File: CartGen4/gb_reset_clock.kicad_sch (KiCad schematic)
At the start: 7 parts, among them SW1 SW_Push, U2 SN74LV1T34DCKR, U3 SIT8008BI-73-33E-33.333333G

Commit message: Changed most R and C to 0402 size
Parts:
- C18: footprint Capacitor_SMD:C_0603_1608Metric_Pad1.08x0.95mm_HandSolder -> Capacitor_SMD:C_0402_1005Metric_Pad0.74x0.62mm_HandSolder
- R11, R13: footprint Resistor_SMD:R_0603_1608Metric_Pad0.98x0.95mm_HandSolder -> Resistor_SMD:R_0402_1005Metric_Pad0.72x0.64mm_HandSolder
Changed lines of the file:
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@@
     (property "Reference" "R13" (id 0) (at 57.15 54.61 90))
     (property "Value" "1K" (id 1) (at 57.15 57.15 90))
-    (property "Footprint" "Resistor_SMD:R_0603_1608Metric_Pad0.98x0.95mm_HandSolder" (id 2) (at 57.15 62.738 90)
+    (property "Footprint" "Resistor_SMD:R_0402_1005Metric_Pad0.72x0.64mm_HandSolder" (id 2) (at 57.15 62.738 90)
       (effects (font (size 1.27 1.27)) hide)
     )
@@
       (effects (font (size 1.27 1.27)) (justify left))
     )
-    (property "Footprint" "Capacitor_SMD:C_0603_1608Metric_Pad1.08x0.95mm_HandSolder" (id 2) (at 112.7252 73.66 0)
+    (property "Footprint" "Capacitor_SMD:C_0402_1005Metric_Pad0.74x0.62mm_HandSolder" (id 2) (at 112.7252 73.66 0)
       (effects (font (size 1.27 1.27)) hide)
     )
@@
       (effects (font (size 1.27 1.27)) (justify right))
     )
-    (property "Footprint" "Resistor_SMD:R_0603_1608Metric_Pad0.98x0.95mm_HandSolder" (id 2) (at 53.848 127 90)
-      (effects (font (size 1.27 1.27)) hide)
-    )
+    (property "Footprint" "Resistor_SMD:R_0402_1005Metric_Pad0.72x0.64mm_HandSolder" (id 2) (at 53.848 127 90)
+      (effects (font (size 1.27 1.27)) hide)
+    )

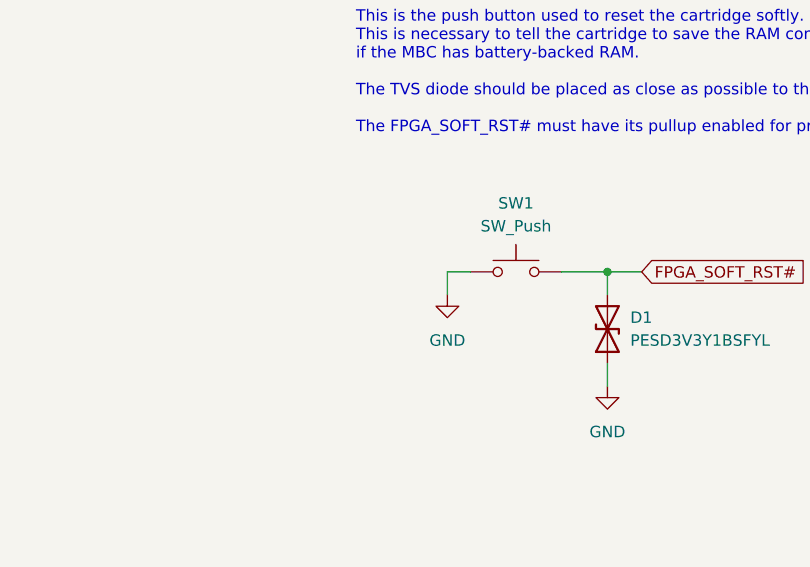
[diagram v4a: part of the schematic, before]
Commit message: Wired general purpose signals
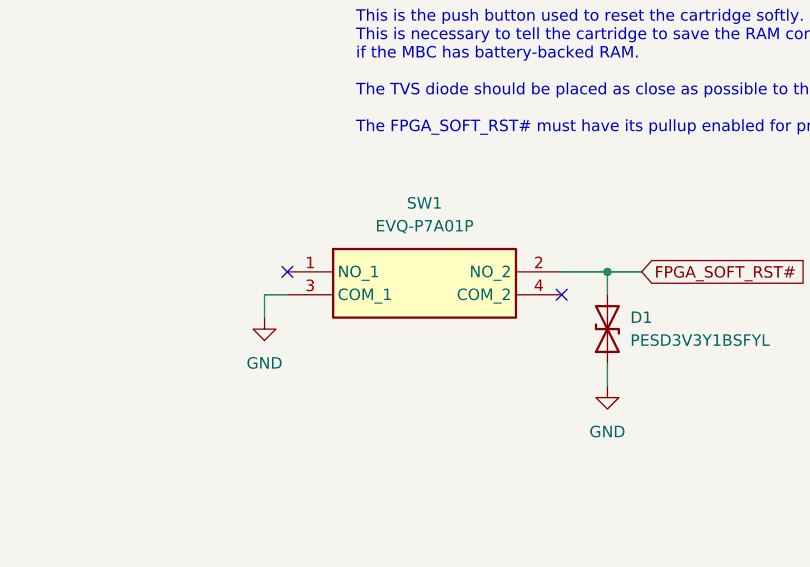
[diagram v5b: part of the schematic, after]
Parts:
- removed SW1: SW_Push, Button_Switch_SMD:SW_SPST_TL3305A, symbol Switch:SW_Push
- added SW1: EVQ-P7A01P, SamacSys_Parts:EVQP7J01P, symbol SamacSys_Parts:EVQ-P7A01P
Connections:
- net FPGA_SOFT_RST#: now also SW1.2 (NO_2)
- net GND: now also SW1.3 (COM_1)
- no-connect marks 0 -> 2
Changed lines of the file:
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@@
   (junction (at 52.07 120.65) (diameter 0) (color 0 0 0 0)
   )
+  (no_connect (at 163.83 66.04))
+  (no_connect (at 194.31 68.58))
   (wire (pts (xy 90.17 63.5) (xy 92.71 63.5))
     (stroke (width 0) (type default) (color 0 0 0 0))
@@
     (stroke (width 0) (type default) (color 0 0 0 0))
   )
-  (wire (pts (xy 181.61 66.04) (xy 181.61 68.58))
-    (stroke (width 0) (type default) (color 0 0 0 0))
-  )
-  (wire (pts (xy 184.15 66.04) (xy 181.61 66.04))
+  (wire (pts (xy 161.29 68.58) (xy 161.29 71.12))
+    (stroke (width 0) (type default) (color 0 0 0 0))
+  )
+  (wire (pts (xy 163.83 68.58) (xy 161.29 68.58))
     (stroke (width 0) (type default) (color 0 0 0 0))
   )
@@
     (pin "1")
   )
-  (symbol (lib_id "power:GND") (at 181.61 68.58 0) (unit 1)
-    (in_bom yes) (on_board yes) (fields_autoplaced)
-    (property "Reference" "#PWR036" (id 0) (at 181.61 74.93 0)
-      (effects (font (size 1.27 1.27)) hide)
-    )
-    (property "Value" "GND" (id 1) (at 181.61 73.66 0))
-    (property "Footprint" "" (id 2) (at 181.61 68.58 0)
-      (effects (font (size 1.27 1.27)) hide)
-    )
-    (property "Datasheet" "" (id 3) (at 181.61 68.58 0)
+  (symbol (lib_id "power:GND") (at 161.29 71.12 0) (unit 1)
+    (in_bom yes) (on_board yes) (fields_autoplaced)
+    (property "Reference" "#PWR036" (id 0) (at 161.29 77.47 0)
+      (effects (font (size 1.27 1.27)) hide)
+    )
+    (property "Value" "GND" (id 1) (at 161.29 76.2 0))
+    (property "Footprint" "" (id 2) (at 161.29 71.12 0)
+      (effects (font (size 1.27 1.27)) hide)
+    )
+    (property "Datasheet" "" (id 3) (at 161.29 71.12 0)
       (effects (font (size 1.27 1.27)) hide)
     )
@@
     (pin "1")
   )
-  (symbol (lib_id "Switch:SW_Push") (at 189.23 66.04 0) (unit 1)
-    (in_bom yes) (on_board yes) (fields_autoplaced)
-    (property "Reference" "SW1" (id 0) (at 189.23 58.42 0))
-    (property "Value" "SW_Push" (id 1) (at 189.23 60.96 0))
-    (property "Footprint" "Button_Switch_SMD:SW_SPST_TL3305A" (id 2) (at 189.23 60.96 0)
-      (effects (font (size 1.27 1.27)) hide)
-    )
-    (property "Datasheet" "~" (id 3) (at 189.23 60.96 0)
-      (effects (font (size 1.27 1.27)) hide)
-    )
-    (property "Critical" "Y" (id 4) (at 189.23 66.04 0)
-      (effects (font (size 1.27 1.27)) hide)
-    )
-    (pin "1")
-    (pin "2")
-  )
   (symbol (lib_id "power:GND") (at 199.39 78.74 0) (unit 1)
     (in_bom yes) (on_board yes) (fields_autoplaced)
@@
     (pin "2")
   )
+  (symbol (lib_id "SamacSys_Parts:EVQ-P7A01P") (at 163.83 66.04 0) (unit 1)
+    (in_bom yes) (on_board yes) (fields_autoplaced)
+    (property "Reference" "SW1" (id 0) (at 179.07 58.42 0))
+    (property "Value" "EVQ-P7A01P" (id 1) (at 179.07 60.96 0))
+    (property "Footprint" "SamacSys_Parts:EVQP7J01P" (id 2) (at 163.83 66.04 0)
+      (effects (font (size 1.27 1.27)) hide)
+    )
+    (property "Datasheet" "" (id 3) (at 163.83 66.04 0)
+      (effects (font (size 1.27 1.27)) hide)
+    )
+    (property "Reference_1" "S" (id 4) (at 179.07 60.96 0)
+      (effects (font (size 1.27 1.27)) hide)
+    )
+    (property "Value_1" "EVQ-P7A01P" (id 5) (at 179.07 60.96 0)
+      (effects (font (size 1.27 1.27)) hide)
+    )
+    (property "Footprint_1" "EVQP7J01P" (id 6) (at 190.5 160.96 0)
+      (effects (font (size 1.27 1.27)) (justify left top) hide)
+    )
+    (property "Datasheet_1" "https://industrial.panasonic.com/cdbs/www-data/pdf/ATK0000/ATK0000C378.pdf" (id 7) (at 190.5 260.96 0)
+      (effects (font (size 1.27 1.27)) (justify left top) hide)
+    )
+    (property "Height" "1" (id 8) (at 190.5 460.96 0)
+      (effects (font (size 1.27 1.27)) (justify left top) hide)
+    )
+    (property "Mouser Part Number" "667-EVQP7A01P" (id 9) (at 190.5 560.96 0)
+      (effects (font (size 1.27 1.27)) (justify left top) hide)
+    )
+    (property "Mouser Price/Stock" "https://www.mouser.co.uk/ProductDetail/Panasonic/EVQ-P7A01P?qs=rJ%252BziJWpysz7n3C20u6WAw%3D%3D" (id 10) (at 190.5 660.96 0)
+      (effects (font (size 1.27 1.27)) (justify left top) hide)
+    )
+    (property "Manufacturer_Name" "Panasonic" (id 11) (at 190.5 760.96 0)
+      (effects (font (size 1.27 1.27)) (justify left top) hide)
+    )
+    (property "Manufacturer_Part_Number" "EVQ-P7A01P" (id 12) (at 190.5 860.96 0)
+      (effects (font (size 1.27 1.27)) (justify left top) hide)
+    )
+    (pin "1")
+    (pin "2")
+    (pin "3")
+    (pin "4")
+  )
   (symbol (lib_id "power:+1V8") (at 111.76 58.42 0) (unit 1)

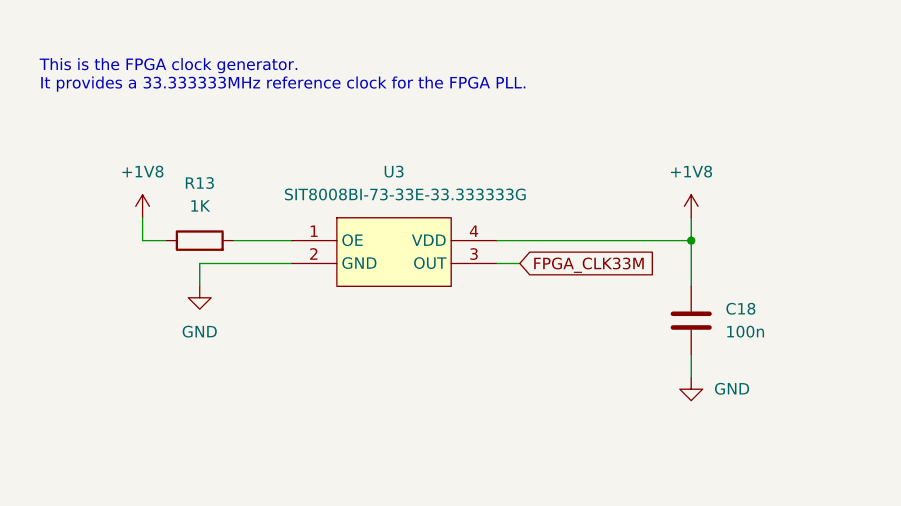
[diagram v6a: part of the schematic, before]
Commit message: Fixed GB_BUS_EN not being on 3V3 bank Added CLK_EN to ext clock
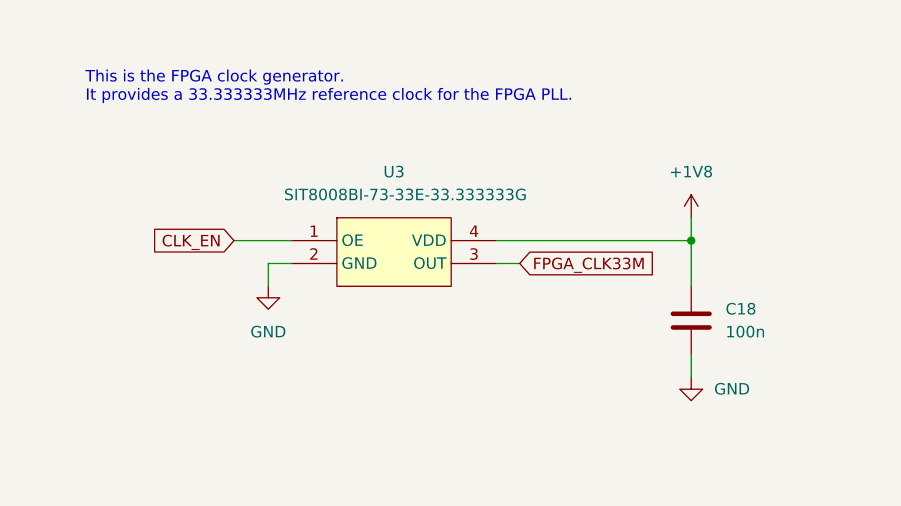
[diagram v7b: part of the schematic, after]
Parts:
- removed R13: 1K, Resistor_SMD:R_0402_1005Metric_Pad0.72x0.64mm_HandSolder, symbol Device:R
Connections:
- net CLK_EN: now reaches U3.1 (OE)
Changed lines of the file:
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@@
   (no_connect (at 163.83 66.04))
   (no_connect (at 194.31 68.58))
+  (wire (pts (xy 67.31 63.5) (xy 64.77 63.5))
+    (stroke (width 0) (type default) (color 0 0 0 0))
+  )
   (wire (pts (xy 90.17 63.5) (xy 92.71 63.5))
     (stroke (width 0) (type default) (color 0 0 0 0))
@@
     (stroke (width 0) (type default) (color 0 0 0 0))
   )
-  (wire (pts (xy 53.34 60.96) (xy 50.8 60.96))
-    (stroke (width 0) (type default) (color 0 0 0 0))
-  )
   (wire (pts (xy 111.76 60.96) (xy 111.76 58.42))
     (stroke (width 0) (type default) (color 0 0 0 0))
   )
+  (wire (pts (xy 199.39 66.04) (xy 199.39 68.58))
+    (stroke (width 0) (type default) (color 0 0 0 0))
+  )
+  (wire (pts (xy 199.39 66.04) (xy 203.2 66.04))
+    (stroke (width 0) (type default) (color 0 0 0 0))
+  )
+  (wire (pts (xy 64.77 63.5) (xy 64.77 66.04))
+    (stroke (width 0) (type default) (color 0 0 0 0))
+  )
+  (wire (pts (xy 119.38 120.65) (xy 119.38 118.11))
+    (stroke (width 0) (type default) (color 0 0 0 0))
+  )
+  (wire (pts (xy 66.04 123.19) (xy 62.23 123.19))
+    (stroke (width 0) (type default) (color 0 0 0 0))
+  )
+  (wire (pts (xy 111.76 73.66) (xy 111.76 76.2))
+    (stroke (width 0) (type default) (color 0 0 0 0))
+  )
+  (wire (pts (xy 111.76 60.96) (xy 111.76 66.04))
+    (stroke (width 0) (type default) (color 0 0 0 0))
+  )
+  (wire (pts (xy 52.07 130.81) (xy 52.07 133.35))
+    (stroke (width 0) (type default) (color 0 0 0 0))
+  )
+  (wire (pts (xy 199.39 76.2) (xy 199.39 78.74))
+    (stroke (width 0) (type default) (color 0 0 0 0))
+  )
+  (wire (pts (xy 91.44 118.11) (xy 95.25 118.11))
+    (stroke (width 0) (type default) (color 0 0 0 0))
+  )
+  (wire (pts (xy 52.07 123.19) (xy 52.07 120.65))
+    (stroke (width 0) (type default) (color 0 0 0 0))
+  )
+  (wire (pts (xy 52.07 133.35) (xy 62.23 133.35))
+    (stroke (width 0) (type default) (color 0 0 0 0))
+  )
   (wire (pts (xy 60.96 60.96) (xy 67.31 60.96))
     (stroke (width 0) (type default) (color 0 0 0 0))
   )
-  (wire (pts (xy 199.39 66.04) (xy 199.39 68.58))
-    (stroke (width 0) (type default) (color 0 0 0 0))
-  )
-  (wire (pts (xy 50.8 60.96) (xy 50.8 58.42))
-    (stroke (width 0) (type default) (color 0 0 0 0))
-  )
-  (wire (pts (xy 199.39 66.04) (xy 203.2 66.04))
-    (stroke (width 0) (type default) (color 0 0 0 0))
-  )
-  (wire (pts (xy 119.38 120.65) (xy 119.38 118.11))
-    (stroke (width 0) (type default) (color 0 0 0 0))
-  )
-  (wire (pts (xy 66.04 123.19) (xy 62.23 123.19))
-    (stroke (width 0) (type default) (color 0 0 0 0))
-  )
-  (wire (pts (xy 67.31 63.5) (xy 57.15 63.5))
-    (stroke (width 0) (type default) (color 0 0 0 0))
-  )
-  (wire (pts (xy 111.76 73.66) (xy 111.76 76.2))
-    (stroke (width 0) (type default) (color 0 0 0 0))
-  )
-  (wire (pts (xy 111.76 60.96) (xy 111.76 66.04))
-    (stroke (width 0) (type default) (color 0 0 0 0))
-  )
-  (wire (pts (xy 52.07 130.81) (xy 52.07 133.35))
-    (stroke (width 0) (type default) (color 0 0 0 0))
-  )
-  (wire (pts (xy 199.39 76.2) (xy 199.39 78.74))
-    (stroke (width 0) (type default) (color 0 0 0 0))
-  )
-  (wire (pts (xy 91.44 118.11) (xy 95.25 118.11))
-    (stroke (width 0) (type default) (color 0 0 0 0))
-  )
-  (wire (pts (xy 52.07 123.19) (xy 52.07 120.65))
-    (stroke (width 0) (type default) (color 0 0 0 0))
-  )
-  (wire (pts (xy 52.07 133.35) (xy 62.23 133.35))
-    (stroke (width 0) (type default) (color 0 0 0 0))
-  )
   (wire (pts (xy 91.44 120.65) (xy 119.38 120.65))
     (stroke (width 0) (type default) (color 0 0 0 0))
@@
   )
   (wire (pts (xy 163.83 68.58) (xy 161.29 68.58))
-    (stroke (width 0) (type default) (color 0 0 0 0))
-  )
-  (wire (pts (xy 57.15 63.5) (xy 57.15 66.04))
     (stroke (width 0) (type default) (color 0 0 0 0))
   )
@@
   )
   (text "This is the FPGA clock generator.\nIt provides a 33.333333MHz reference clock for the FPGA PLL."
-    (at 39.37 44.45 0)
+    (at 44.45 45.72 0)
     (effects (font (size 1.27 1.27)) (justify left bottom))
   )
@@
     (property "Intersheet References" "${INTERSHEET_REFS}" (id 0) (at 108.2464 63.4206 0)
       (effects (font (size 1.27 1.27)) (justify left) hide)
+    )
+  )
+  (global_label "CLK_EN" (shape input) (at 60.96 60.96 180) (fields_autoplaced)
+    (effects (font (size 1.27 1.27)) (justify right))
+    (property "Intersheet References" "${INTERSHEET_REFS}" (id 0) (at 51.5317 60.8806 0)
+      (effects (font (size 1.27 1.27)) (justify right) hide)
     )
   )
@@
     )
     (property "Voltage" "3.3V" (id 11) (at 199.39 72.39 0)
-      (effects (font (size 1.27 1.27)) hide)
-    )
-    (pin "1")
-    (pin "2")
-  )
-  (symbol (lib_id "power:GND") (at 57.15 66.04 0) (unit 1)
-    (in_bom yes) (on_board yes) (fields_autoplaced)
-    (property "Reference" "#PWR032" (id 0) (at 57.15 72.39 0)
-      (effects (font (size 1.27 1.27)) hide)
-    )
-    (property "Value" "GND" (id 1) (at 57.15 71.12 0))
-    (property "Footprint" "" (id 2) (at 57.15 66.04 0)
-      (effects (font (size 1.27 1.27)) hide)
-    )
-    (property "Datasheet" "" (id 3) (at 57.15 66.04 0)
-      (effects (font (size 1.27 1.27)) hide)
-    )
-    (pin "1")
-  )
-  (symbol (lib_id "Device:R") (at 57.15 60.96 90) (unit 1)
-    (in_bom yes) (on_board yes) (fields_autoplaced)
-    (property "Reference" "R13" (id 0) (at 57.15 54.61 90))
-    (property "Value" "1K" (id 1) (at 57.15 57.15 90))
-    (property "Footprint" "Resistor_SMD:R_0402_1005Metric_Pad0.72x0.64mm_HandSolder" (id 2) (at 57.15 62.738 90)
-      (effects (font (size 1.27 1.27)) hide)
-    )
-    (property "Datasheet" "~" (id 3) (at 57.15 60.96 0)
-      (effects (font (size 1.27 1.27)) hide)
-    )
-    (property "Tolerance" "10%" (id 4) (at 57.15 60.96 0)
-      (effects (font (size 1.27 1.27)) hide)
-    )
-    (property "Source" "ANY" (id 5) (at 57.15 60.96 0)
-      (effects (font (size 1.27 1.27)) hide)
-    )
-    (property "Critical" "Y" (id 6) (at 57.15 60.96 0)
       (effects (font (size 1.27 1.27)) hide)
     )
@@
     (pin "5")
   )
-  (symbol (lib_id "power:+1V8") (at 50.8 58.42 0) (unit 1)
+  (symbol (lib_id "power:GND") (at 64.77 66.04 0) (unit 1)
     (in_bom yes) (on_board yes) (fields_autoplaced)
-    (property "Reference" "#PWR031" (id 0) (at 50.8 62.23 0)
-      (effects (font (size 1.27 1.27)) hide)
-    )
-    (property "Value" "+1V8" (id 1) (at 50.8 53.34 0))
-    (property "Footprint" "" (id 2) (at 50.8 58.42 0)
-      (effects (font (size 1.27 1.27)) hide)
-    )
-    (property "Datasheet" "" (id 3) (at 50.8 58.42 0)
-      (effects (font (size 1.27 1.27)) hide)
-    )
+    (property "Reference" "#PWR0114" (id 0) (at 64.77 72.39 0)
+      (effects (font (size 1.27 1.27)) hide)
+    )
+    (property "Value" "GND" (id 1) (at 64.77 71.12 0))
+    (property "Footprint" "" (id 2) (at 64.77 66.04 0)
+      (effects (font (size 1.27 1.27)) hide)
+    )
+    (property "Datasheet" "" (id 3) (at 64.77 66.04 0)
+      (effects (font (size 1.27 1.27)) hide)
+    )

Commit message: Updated field information
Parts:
- C18: Package ID (none) -> 0402
- R11: Notes (none) -> Pulldown resistor for GB_RST# line to ensure GB remains in 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; Package ID (none) -> 0402
- SW1: Critical (none) -> Y; Datasheet_1 https://industrial.panasonic.com/cdbs/www-data/pdf/ATK0000/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 -> (none); Footprint_1 EVQP7J01P -> (none); MFN (none) -> Panasonic; MFP (none) -> EVQ-P7A01P; Manufacturer_Name Panasonic -> (none); Manufacturer_Part_Number EVQ-P7A01P -> (none); Mouser Part Number 667-EVQP7A01P -> (none); Mouser Price/Stock https://www.mouser.co.uk/ProductDetail/Panasonic/EVQ-P7A01P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 -> (none); Notes (none) -> Reset button for gracefull shutdown of game (for saving gam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; Reference_1 S -> (none); Source (none) -> SPEC; Value_1 EVQ-P7A01P -> (none)
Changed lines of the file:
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@@
+      (effects (font (size 1.27 1.27)) hide)
+    )
+    (property "Description" "~" (id 7) (at 111.76 69.85 0)
+      (effects (font (size 1.27 1.27)) hide)
+    )
+    (property "MFN" "~" (id 8) (at 111.76 69.85 0)
+      (effects (font (size 1.27 1.27)) hide)
+    )
+    (property "MFP" "~" (id 9) (at 111.76 69.85 0)
+      (effects (font (size 1.27 1.27)) hide)
+    )
+    (property "Package ID" "0402" (id 10) (at 111.76 69.85 0)
       (effects (font (size 1.27 1.27)) hide)
     )
@@
       (effects (font (size 1.27 1.27)) hide)
     )
+    (property "Notes" "Pulldown resistor for GB_RST# line to ensure GB remains in reset while the cart is initialising" (id 7) (at 52.07 127 0)
+      (effects (font (size 1.27 1.27)) hide)
+    )
+    (property "Description" "~" (id 8) (at 52.07 127 0)
+      (effects (font (size 1.27 1.27)) hide)
+    )
+    (property "MFN" "~" (id 9) (at 52.07 127 0)
+      (effects (font (size 1.27 1.27)) hide)
+    )
+    (property "MFP" "~" (id 10) (at 52.07 127 0)
+      (effects (font (size 1.27 1.27)) hide)
+    )
+    (property "Package ID" "0402" (id 11) (at 52.07 127 0)
+      (effects (font (size 1.27 1.27)) hide)
+    )
     (pin "1")
     (pin "2")
@@
       (effects (font (size 1.27 1.27)) hide)
     )
-    (property "Datasheet" "" (id 3) (at 163.83 66.04 0)
+    (property "Datasheet" "https://industrial.panasonic.com/cdbs/www-data/pdf/ATK0000/ATK0000C378.pdf" (id 3) (at 163.83 66.04 0)
       (effects (font (size 1.27 1.27)) hide)
-    )
-    (property "Reference_1" "S" (id 4) (at 179.07 60.96 0)
-      (effects (font (size 1.27 1.27)) hide)
-    )
-    (property "Value_1" "EVQ-P7A01P" (id 5) (at 179.07 60.96 0)
-      (effects (font (size 1.27 1.27)) hide)
-    )
-    (property "Footprint_1" "EVQP7J01P" (id 6) (at 190.5 160.96 0)
-      (effects (font (size 1.27 1.27)) (justify left top) hide)
-    )
-    (property "Datasheet_1" "https://industrial.panasonic.com/cdbs/www-data/pdf/ATK0000/ATK0000C378.pdf" (id 7) (at 190.5 260.96 0)
-      (effects (font (size 1.27 1.27)) (justify left top) hide)
     )
     (property "Height" "1" (id 8) (at 190.5 460.96 0)
       (effects (font (size 1.27 1.27)) (justify left top) hide)
     )
-    (property "Mouser Part Number" "667-EVQP7A01P" (id 9) (at 190.5 560.96 0)
-      (effects (font (size 1.27 1.27)) (justify left top) hide)
+    (property "MFN" "Panasonic" (id 13) (at 163.83 66.04 0)
+      (effects (font (size 1.27 1.27)) hide)
     )
-    (property "Mouser Price/Stock" "https://www.mouser.co.uk/ProductDetail/Panasonic/EVQ-P7A01P?qs=rJ%252BziJWpysz7n3C20u6WAw%3D%3D" (id 10) (at 190.5 660.96 0)
-      (effects (font (size 1.27 1.27)) (justify left top) hide)
+    (property "MFP" "EVQ-P7A01P" (id 13) (at 163.83 66.04 0)
+      (effects (font (size 1.27 1.27)) hide)
     )
-    (property "Manufacturer_Name" "Panasonic" (id 11) (at 190.5 760.96 0)
-      (effects (font (size 1.27 1.27)) (justify left top) hide)
+    (property "Notes" "Reset button for gracefull shutdown of game (for saving game data)" (id 14) (at 163.83 66.04 0)
+      (effects (font (size 1.27 1.27)) hide)
     )
-    (property "Manufacturer_Part_Number" "EVQ-P7A01P" (id 12) (at 190.5 860.96 0)
-      (effects (font (size 1.27 1.27)) (justify left top) hide)
+    (property "Description" "Tactile Switches 3.5x2.9mm Right Ang Light Touch Switch" (id 15) (at 163.83 66.04 0)
+      (effects (font (size 1.27 1.27)) hide)
+    )
+    (property "Source" "SPEC" (id 16) (at 163.83 66.04 0)
+      (effects (font (size 1.27 1.27)) hide)
+    )
+    (property "Critical" "Y" (id 17) (at 163.83 66.04 0)
+      (effects (font (size 1.27 1.27)) hide)
+    )
+    (property "Package ID" "~" (id 18) (at 163.83 66.04 0)
+      (effects (font (size 1.27 1.27)) hide)
     )
     (pin "1")
